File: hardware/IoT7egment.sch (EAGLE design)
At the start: 16 parts, among them IC1 74HCT595N, IC2 74HCT595N

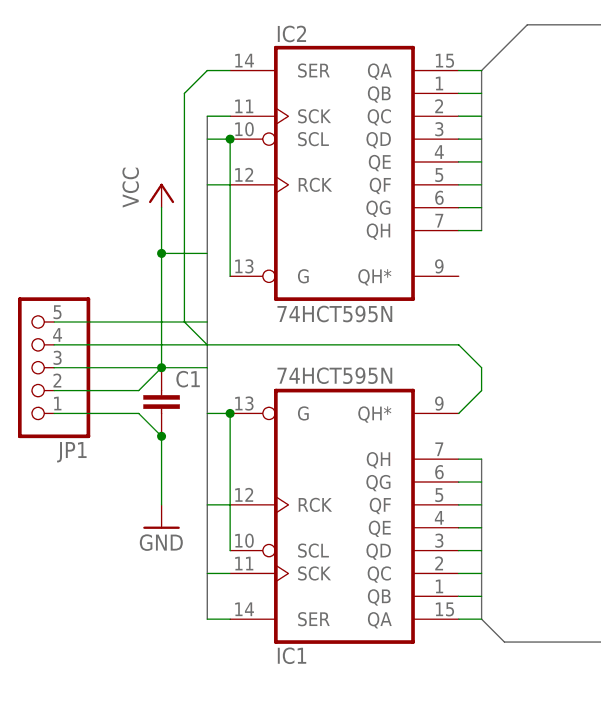
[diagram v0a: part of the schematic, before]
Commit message: rectified the active low enable pin connection in schematic resolve #1
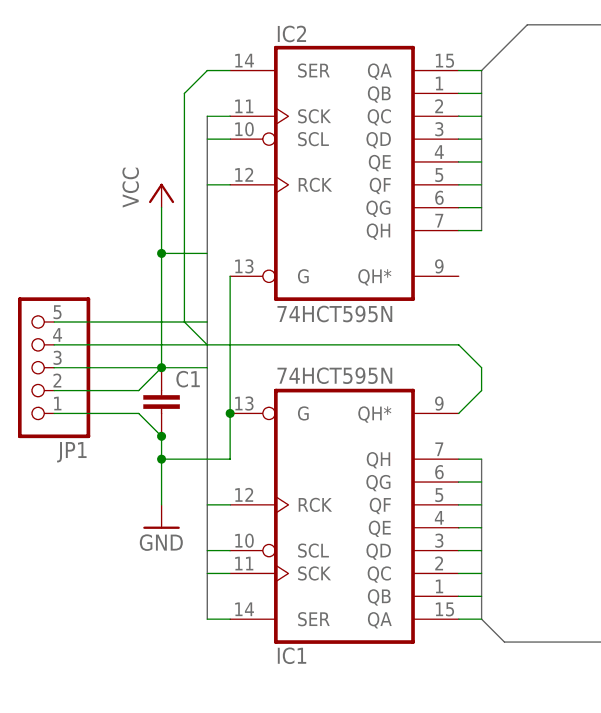
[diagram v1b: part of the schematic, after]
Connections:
- net GND: now also IC1A.G, IC2A.G
- net SER3: no longer IC1A.G, IC2A.G
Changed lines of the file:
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@@
 <?xml version="1.0" encoding="utf-8"?>
 <!DOCTYPE eagle SYSTEM "eagle.dtd">
-<eagle version="6.5.0">
+<eagle version="7.1.0">
 <drawing>
 <settings>
@@
 <setting verticaltext="up"/>
 </settings>
-<grid distance="0.1" unitdist="inch" unit="inch" style="lines" multiple="1" display="yes" altdistance="0.01" altunitdist="inch" altunit="inch"/>
+<grid distance="0.1" unitdist="inch" unit="inch" style="lines" multiple="1" display="no" altdistance="0.01" altunitdist="inch" altunit="inch"/>
 <layers>
-<layer number="1" name="Top" color="4" fill="1" visible="yes" active="no"/>
-<layer number="2" name="Route2" color="1" fill="3" visible="yes" active="no"/>
-<layer number="3" name="Route3" color="4" fill="3" visible="yes" active="no"/>
-<layer number="4" name="Route4" color="1" fill="4" visible="yes" active="no"/>
-<layer number="5" name="Route5" color="4" fill="4" visible="yes" active="no"/>
-<layer number="6" name="Route6" color="1" fill="8" visible="yes" active="no"/>
-<layer number="7" name="Route7" color="4" fill="8" visible="yes" active="no"/>
-<layer number="8" name="Route8" color="1" fill="2" visible="yes" active="no"/>
-<layer number="9" name="Route9" color="4" fill="2" visible="yes" active="no"/>
-<layer number="10" name="Route10" color="1" fill="7" visible="yes" active="no"/>
-<layer number="11" name="Route11" color="4" fill="7" visible="yes" active="no"/>
-<layer number="12" name="Route12" color="1" fill="5" visible="yes" active="no"/>
-<layer number="13" name="Route13" color="4" fill="5" visible="yes" active="no"/>
-<layer number="14" name="Route14" color="1" fill="6" visible="yes" active="no"/>
-<layer number="15" name="Route15" color="4" fill="6" visible="yes" active="no"/>
-<layer number="16" name="Bottom" color="1" fill="1" visible="yes" active="no"/>
-<layer number="17" name="Pads" color="2" fill="1" visible="yes" active="no"/>
-<layer number="18" name="Vias" color="2" fill="1" visible="yes" active="no"/>
-<layer number="19" name="Unrouted" color="6" fill="1" visible="yes" active="no"/>
-<layer number="20" name="Dimension" color="15" fill="1" visible="yes" active="no"/>
-<layer number="21" name="tPlace" color="7" fill="1" visible="yes" active="no"/>
-<layer number="22" name="bPlace" color="7" fill="1" visible="yes" active="no"/>
-<layer number="23" name="tOrigins" color="15" fill="1" visible="yes" active="no"/>
-<layer number="24" name="bOrigins" color="15" fill="1" visible="yes" active="no"/>
-<layer number="25" name="tNames" color="7" fill="1" visible="yes" active="no"/>
-<layer number="26" name="bNames" color="7" fill="1" visible="yes" active="no"/>
-<layer number="27" name="tValues" color="7" fill="1" visible="yes" active="no"/>
-<layer number="28" name="bValues" color="7" fill="1" visible="yes" active="no"/>
+<layer number="1" name="Top" color="4" fill="1" visible="no" active="no"/>
+<layer number="2" name="Route2" color="1" fill="3" visible="no" active="no"/>
+<layer number="3" name="Route3" color="4" fill="3" visible="no" active="no"/>
+<layer number="4" name="Route4" color="1" fill="4" visible="no" active="no"/>
+<layer number="5" name="Route5" color="4" fill="4" visible="no" active="no"/>
+<layer number="6" name="Route6" color="1" fill="8" visible="no" active="no"/>
+<layer number="7" name="Route7" color="4" fill="8" visible="no" active="no"/>
+<layer number="8" name="Route8" color="1" fill="2" visible="no" active="no"/>
+<layer number="9" name="Route9" color="4" fill="2" visible="no" active="no"/>
+<layer number="10" name="Route10" color="1" fill="7" visible="no" active="no"/>
+<layer number="11" name="Route11" color="4" fill="7" visible="no" active="no"/>
+<layer number="12" name="Route12" color="1" fill="5" visible="no" active="no"/>
+<layer number="13" name="Route13" color="4" fill="5" visible="no" active="no"/>
+<layer number="14" name="Route14" color="1" fill="6" visible="no" active="no"/>
+<layer number="15" name="Route15" color="4" fill="6" visible="no" active="no"/>
+<layer number="16" name="Bottom" color="1" fill="1" visible="no" active="no"/>
+<layer number="17" name="Pads" color="2" fill="1" visible="no" active="no"/>
+<layer number="18" name="Vias" color="2" fill="1" visible="no" active="no"/>
+<layer number="19" name="Unrouted" color="6" fill="1" visible="no" active="no"/>
+<layer number="20" name="Dimension" color="15" fill="1" visible="no" active="no"/>
+<layer number="21" name="tPlace" color="7" fill="1" visible="no" active="no"/>
+<layer number="22" name="bPlace" color="7" fill="1" visible="no" active="no"/>
+<layer number="23" name="tOrigins" color="15" fill="1" visible="no" active="no"/>
+<layer number="24" name="bOrigins" color="15" fill="1" visible="no" active="no"/>
+<layer number="25" name="tNames" color="7" fill="1" visible="no" active="no"/>
+<layer number="26" name="bNames" color="7" fill="1" visible="no" active="no"/>
+<layer number="27" name="tValues" color="7" fill="1" visible="no" active="no"/>
+<layer number="28" name="bValues" color="7" fill="1" visible="no" active="no"/>
 <layer number="29" name="tStop" color="7" fill="3" visible="no" active="no"/>
 <layer number="30" name="bStop" color="7" fill="6" visible="no" active="no"/>
@@
 <layer number="35" name="tGlue" color="7" fill="4" visible="no" active="no"/>
 <layer number="36" name="bGlue" color="7" fill="5" visible="no" active="no"/>
-<layer number="37" name="tTest" color="7" fill="1" visible="yes" active="no"/>
-<layer number="38" name="bTest" color="7" fill="1" visible="yes" active="no"/>
+<layer number="37" name="tTest" color="7" fill="1" visible="no" active="no"/>
+<layer number="38" name="bTest" color="7" fill="1" visible="no" active="no"/>
 <layer number="39" name="tKeepout" color="4" fill="11" visible="no" active="no"/>
 <layer number="40" name="bKeepout" color="1" fill="11" visible="no" active="no"/>
@@
 <layer number="44" name="Drills" color="7" fill="1" visible="no" active="no"/>
 <layer number="45" name="Holes" color="7" fill="1" visible="no" active="no"/>
-<layer number="46" name="Milling" color="3" fill="1" visible="yes" active="no"/>
-<layer number="47" name="Measures" color="7" fill="1" visible="yes" active="no"/>
-<layer number="48" name="Document" color="7" fill="1" visible="yes" active="no"/>
-<layer number="49" name="Reference" color="7" fill="1" visible="yes" active="no"/>
-<layer number="50" name="dxf" color="7" fill="1" visible="yes" active="no"/>
-<layer number="51" name="tDocu" color="7" fill="1" visible="yes" active="no"/>
-<layer number="52" name="bDocu" color="7" fill="1" visible="yes" active="no"/>
-<layer number="53" name="tGND_GNDA" color="7" fill="1" visible="yes" active="no"/>
-<layer number="54" name="bGND_GNDA" color="7" fill="1" visible="yes" active="no"/>
+<layer number="46" name="Milling" color="3" fill="1" visible="no" active="no"/>
+<layer number="47" name="Measures" color="7" fill="1" visible="no" active="no"/>
+<layer number="48" name="Document" color="7" fill="1" visible="no" active="no"/>
+<layer number="49" name="Reference" color="7" fill="1" visible="no" active="no"/>
+<layer number="50" name="dxf" color="7" fill="1" visible="no" active="no"/>
+<layer number="51" name="tDocu" color="7" fill="1" visible="no" active="no"/>
+<layer number="52" name="bDocu" color="7" fill="1" visible="no" active="no"/>
+<layer number="53" name="tGND_GNDA" color="7" fill="1" visible="no" active="no"/>
+<layer number="54" name="bGND_GNDA" color="7" fill="1" visible="no" active="no"/>
 <layer number="91" name="Nets" color="2" fill="1" visible="yes" active="yes"/>
 <layer number="92" name="Busses" color="1" fill="1" visible="yes" active="yes"/>
@@
 </segment>
 <segment>
+<pinref part="IC2" gate="A" pin="SCL"/>
+<wire x1="40.64" y1="111.76" x2="38.1" y2="111.76" width="0.1524" layer="91"/>
+</segment>
+<segment>
 <pinref part="IC1" gate="A" pin="SCL"/>
-<pinref part="IC1" gate="A" pin="G"/>
-<wire x1="40.64" y1="66.04" x2="40.64" y2="81.28" width="0.1524" layer="91"/>
-<wire x1="40.64" y1="81.28" x2="38.1" y2="81.28" width="0.1524" layer="91"/>
-<junction x="40.64" y="81.28"/>
-</segment>
-<segment>
-<pinref part="IC2" gate="A" pin="G"/>
-<pinref part="IC2" gate="A" pin="SCL"/>
-<wire x1="40.64" y1="96.52" x2="40.64" y2="111.76" width="0.1524" layer="91"/>
-<wire x1="40.64" y1="111.76" x2="38.1" y2="111.76" width="0.1524" layer="91"/>
-<junction x="40.64" y="111.76"/>
+<wire x1="40.64" y1="66.04" x2="38.1" y2="66.04" width="0.1524" layer="91"/>
 </segment>
 </net>
@@
 <segment>
 <pinref part="GND1" gate="1" pin="GND"/>
-<wire x1="33.02" y1="71.12" x2="33.02" y2="78.74" width="0.1524" layer="91"/>
+<wire x1="33.02" y1="71.12" x2="33.02" y2="76.2" width="0.1524" layer="91"/>
+<wire x1="33.02" y1="76.2" x2="33.02" y2="78.74" width="0.1524" layer="91"/>
 <wire x1="33.02" y1="78.74" x2="30.48" y2="81.28" width="0.1524" layer="91"/>
 <pinref part="JP1" gate="A" pin="1"/>
@@
 <pinref part="C1" gate="G$1" pin="2"/>
 <junction x="33.02" y="78.74"/>
-</segment>
-</net>
+<wire x1="33.02" y1="76.2" x2="40.64" y2="76.2" width="0.1524" layer="91"/>
+<junction x="33.02" y="76.2"/>
+<pinref part="IC2" gate="A" pin="G"/>
+<pinref part="IC1" gate="A" pin="G"/>
+<wire x1="40.64" y1="96.52" x2="40.64" y2="81.28" width="0.1524" layer="91"/>
+<wire x1="40.64" y1="76.2" x2="40.64" y2="81.28" width="0.1524" layer="91"/>
+<junction x="40.64" y="81.28"/>
+</segment>
+</net>
